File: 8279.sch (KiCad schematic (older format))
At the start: 26 parts

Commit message: made final adjustments to all the designes
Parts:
- removed U?: PAL16L8, symbol Logic_Programmable:PAL16L8
- removed U?: 4001, symbol 4xxx:4001
- added C801: 0.1uF, Capacitor_SMD:CP_Elec_3x5.3, symbol Device:C
- added U801: 74LS11, Package_DIP:DIP-14_W7.62mm_SMDSocket_SmallPads, symbol 74xx:74LS11
- added U803: PAL16L8, Package_DIP:DIP-20_W7.62mm_SMDSocket_SmallPads, symbol Logic_Programmable:PAL16L8
- SW801, SW802, SW803, SW804, SW805, SW806, SW807, SW808, SW809, SW810, SW811, SW812, SW813, SW814, SW815, SW816, SW817, SW818, SW819, SW820, SW821, SW822: renamed from SW?; footprint (none) -> Button_Switch_SMD:SW_SPST_B3U-1000P
- U802: renamed from U?; footprint pkd8279 -> parts:pkd8279
- U804: renamed from U?; footprint (none) -> Package_DIP:DIP-16_W7.62mm_SMDSocket_SmallPads
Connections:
- net labels added: IR2, VCC, ~RD, ~WR
- net labels removed: IRQ, RD, WR
- wire segments 225 -> 178
- no-connect marks 64 -> 20

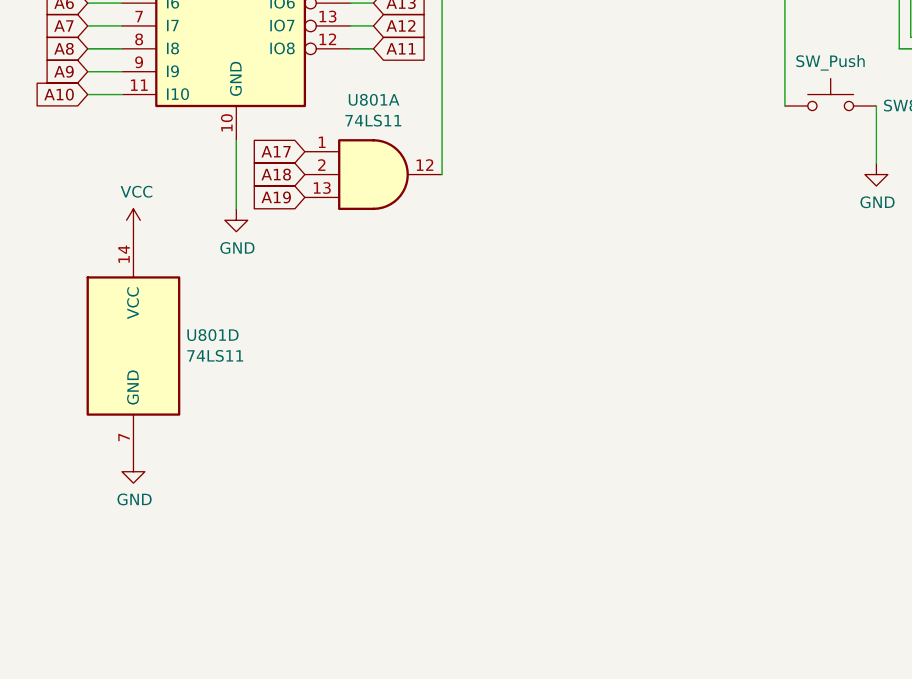
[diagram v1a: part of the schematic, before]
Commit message: adjusted and incorperated 8dipswitch to pcb
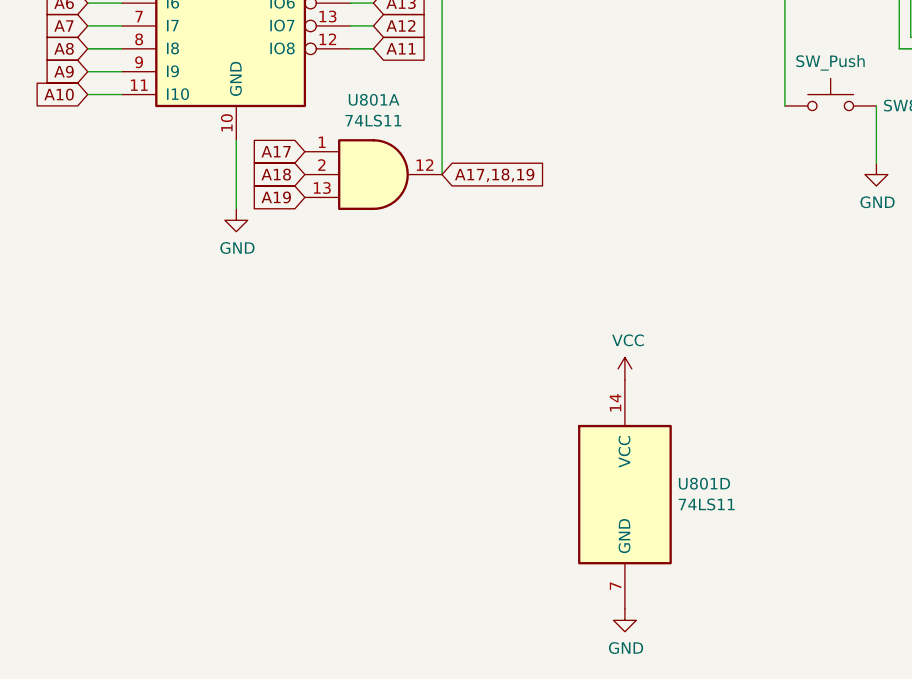
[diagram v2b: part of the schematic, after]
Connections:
- net A17,18,19: now reaches U801.12, U803.18 (IO2)
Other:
- moved on the sheet: U801D
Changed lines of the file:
@@
 $Descr A4 11693 8268
 encoding utf-8
-Sheet 8 8
+Sheet 8 9
 Title ""
 Date ""
@@
 L 74xx:74LS11 U801
 U 4 1 614B183D
-P 950 6750
-F 0 "U801" H 1180 6796 50  0000 L CNN
-F 1 "74LS11" H 1180 6705 50  0000 L CNN
-F 2 "Package_DIP:DIP-14_W7.62mm_SMDSocket_SmallPads" H 950 6750 50  0001 C CNN
-F 3 "http://www.ti.com/lit/gpn/sn74LS11" H 950 6750 50  0001 C CNN
-	4    950  6750
+P 3100 7400
+F 0 "U801" H 3330 7446 50  0000 L CNN
+F 1 "74LS11" H 3330 7355 50  0000 L CNN
+F 2 "Package_DIP:DIP-14_W7.62mm_SMDSocket_SmallPads" H 3100 7400 50  0001 C CNN
+F 3 "http://www.ti.com/lit/gpn/sn74LS11" H 3100 7400 50  0001 C CNN
+	4    3100 7400
 	1    0    0    -1
 $EndComp
@@
 L power:GND #PWR0802
 U 1 1 614B34E0
-P 950 7250
-F 0 "#PWR0802" H 950 7000 50  0001 C CNN
-F 1 "GND" H 955 7077 50  0000 C CNN
-F 2 "" H 950 7250 50  0001 C CNN
-F 3 "" H 950 7250 50  0001 C CNN
-	1    950  7250
+P 3100 7900
+F 0 "#PWR0802" H 3100 7650 50  0001 C CNN
+F 1 "GND" H 3105 7727 50  0000 C CNN
+F 2 "" H 3100 7900 50  0001 C CNN
+F 3 "" H 3100 7900 50  0001 C CNN
+	1    3100 7900
 	1    0    0    -1
 $EndComp
@@
 L power:VCC #PWR0801
 U 1 1 614B3B77
-P 950 6250
-F 0 "#PWR0801" H 950 6100 50  0001 C CNN
-F 1 "VCC" H 965 6423 50  0000 C CNN
-F 2 "" H 950 6250 50  0001 C CNN
-F 3 "" H 950 6250 50  0001 C CNN
-	1    950  6250
-	1    0    0    -1
-$EndComp
+P 3100 6900
+F 0 "#PWR0801" H 3100 6750 50  0001 C CNN
+F 1 "VCC" H 3115 7073 50  0000 C CNN
+F 2 "" H 3100 6900 50  0001 C CNN
+F 3 "" H 3100 6900 50  0001 C CNN
+	1    3100 6900
+	1    0    0    -1
+$EndComp
+Text GLabel 2300 6000 2    50   Input ~ 0
+A17,18,19
 $EndSCHEMATC
